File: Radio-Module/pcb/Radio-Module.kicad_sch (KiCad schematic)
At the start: 0 parts

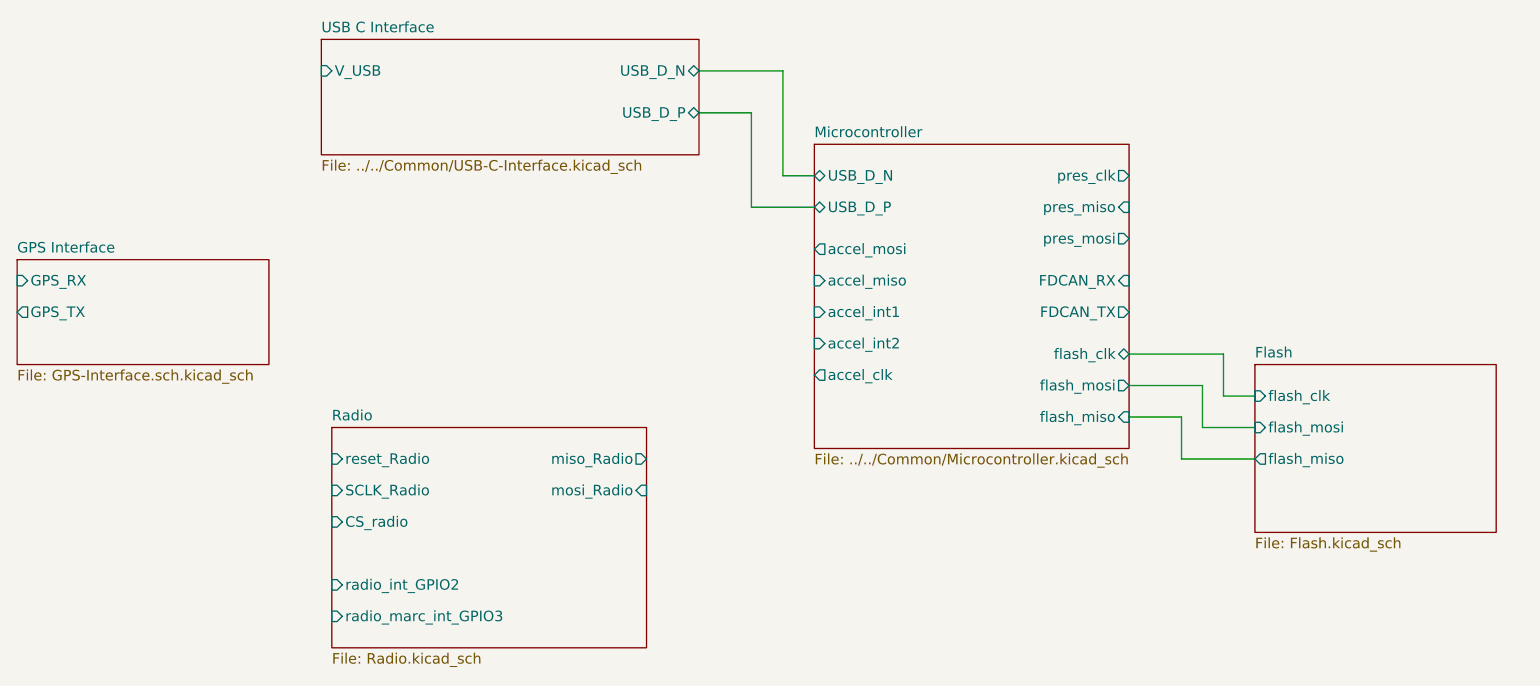
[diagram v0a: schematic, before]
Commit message: Added New MCU to Radio Schematic
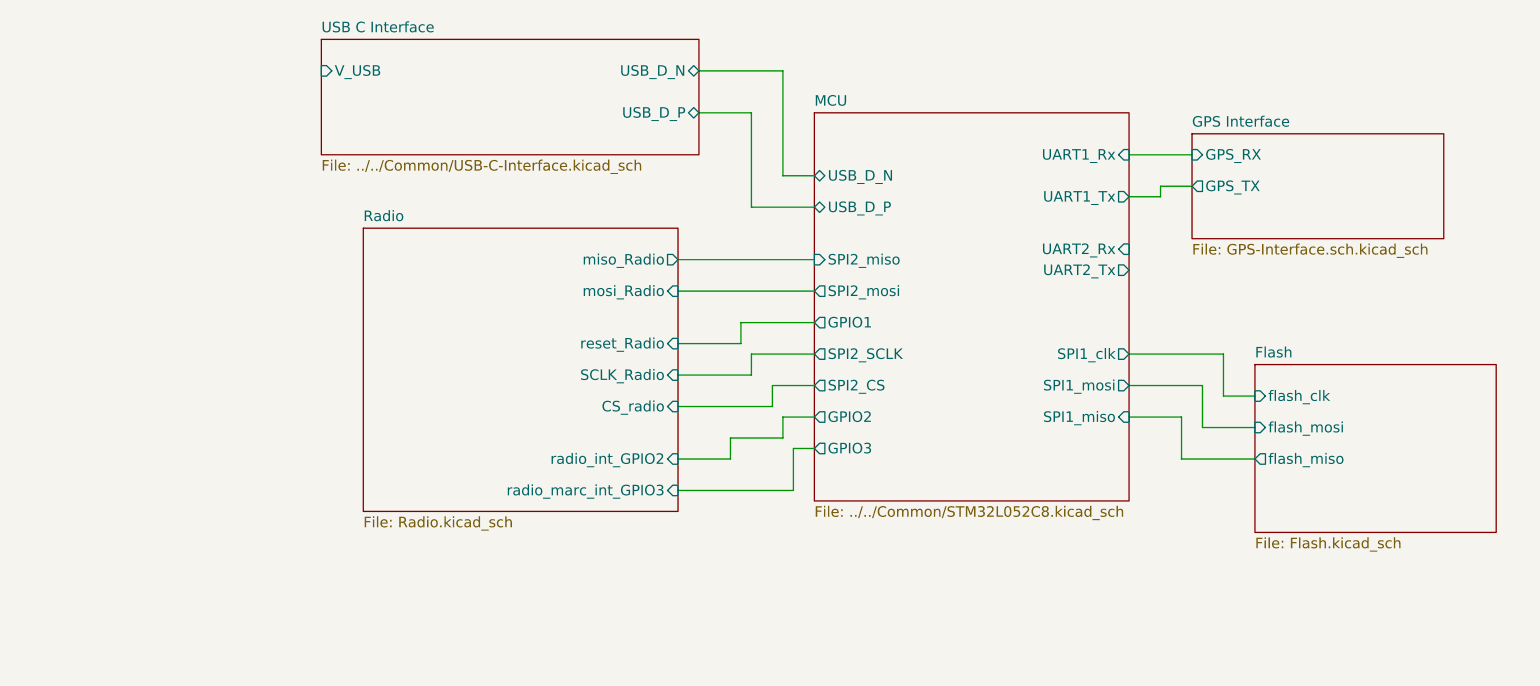
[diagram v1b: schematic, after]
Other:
- removed sheet Microcontroller
- added sheet MCU (../../Common/STM32L052C8.kicad_sch)
